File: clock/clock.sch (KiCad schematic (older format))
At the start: 63 parts, among them J1 Barrel_Jack, SW1 SW_Clock, SW2 CLK_SEL, SW3 SW_Step, SW4 SW_MANUAL_CLK, U1 LM7805, U10 LM555, U2 74LS93, U3 LM556, U4 74LS151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

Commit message: Added switches and redesign
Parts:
- removed C9: 10pF, Capacitor_THT:C_Disc_D3.8mm_W2.6mm_P2.50mm, symbol Device:C
- removed D14, D4: LED_Small, digikey-footprints:LED_3mm_Radial, symbol Device:LED_Small
- removed unit 1 of U5
- removed unit 4 of U5
- removed unit 5 of U5
- removed unit 1 of U6
- removed unit 2 of U7
- removed unit 3 of U7
- removed unit 4 of U7
- removed unit 5 of U7
- added J2: Conn_01x04, Connector_JST:JST_EH_B4B-EH-A_1x04_P2.50mm_Vertical, symbol Connector_Generic:Conn_01x04
- added Q1, Q2, Q3, Q4: 2N3904, Package_TO_SOT_THT:TO-92_Inline, symbol Transistor_BJT:2N3904
- added R17, R18, R19, R20: 1K, Resistor_THT:R_Axial_DIN0207_L6.3mm_D2.5mm_P7.62mm_Horizontal, symbol Device:R
- added RN3: 10K, Resistor_THT:R_Array_SIP5, symbol Device:R_Network04
- added U5: 74LS08, Package_DIP:DIP-14_W7.62mm_Socket, symbol 74xx:74LS08
- added unit 4 of U8
- added unit 5 of U8
- D1, D10, D11, D12, D13, D15, D2, D3, D5, D6, D7, D8, D9: footprint digikey-footprints:LED_3mm_Radial -> LED_THT:LED_D4.0mm
- R16: footprint Resistor_THT:R_Axial_DIN0204_L3.6mm_D1.6mm_P7.62mm_Horizontal -> Resistor_THT:R_Axial_DIN0207_L6.3mm_D2.5mm_P7.62mm_Horizontal
- RN1: value R_Network04 -> 470
- RN2: footprint Resistor_THT:R_Array_SIP6 -> Resistor_THT:R_Array_SIP5; symbol Device:R_Network05 -> Device:R_Network04
- U6: renamed from U7; value 74LS02 -> 74LS32; symbol 74xx:74LS02 -> 74xx:74LS32
- renumbered U5 to U9
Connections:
- net labels removed: PUL3
- wire segments 246 -> 261
- no-connect marks 4 -> 6
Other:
- moved on the sheet: D10, D11, D12, D13, U8A, U8C, U9A, U9B, U9D

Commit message: Fixed plug sizes and foot prints
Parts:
- added D4: D, Diode_THT:D_DO-41_SOD81_P7.62mm_Horizontal, symbol Device:D
- added J3: Power +5V In, Connector_JST:JST_EH_B2B-EH-A_1x02_P2.50mm_Vertical, symbol Connector_Generic:Conn_01x02
- J1: footprint Connector_BarrelJack:BarrelJack_CUI_PJ-063AH_Horizontal -> Connector_BarrelJack:BarrelJack_CUI_PJ-102AH_Horizontal
- J2: footprint Connector_JST:JST_EH_B4B-EH-A_1x04_P2.50mm_Vertical -> Connector_JST:JST_EH_B5B-EH-A_1x05_P2.50mm_Vertical; symbol Connector_Generic:Conn_01x04 -> Connector_Generic:Conn_01x05
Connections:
- wire segments 261 -> 274
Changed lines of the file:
@@
 F 0 "J1" H 850 7500 50  0000 C CNN
 F 1 "Barrel_Jack" H 850 7100 50  0001 C CNN
-F 2 "Connector_BarrelJack:BarrelJack_CUI_PJ-063AH_Horizontal" H 900 7260 50  0001 C CNN
+F 2 "Connector_BarrelJack:BarrelJack_CUI_PJ-102AH_Horizontal" H 900 7260 50  0001 C CNN
 F 3 "~" H 900 7260 50  0001 C CNN
 	1    850  7300
@@
 	3750 3750 4500 3750
 $Comp
-L Connector_Generic:Conn_01x04 J2
+L Connector_Generic:Conn_01x05 J2
 U 1 1 5D4F2577
-P 10050 3000
-F 0 "J2" V 10150 2950 50  0000 L CNN
-F 1 "Conn_01x04" H 10130 2901 50  0001 L CNN
-F 2 "Connector_JST:JST_EH_B4B-EH-A_1x04_P2.50mm_Vertical" H 10050 3000 50  0001 C CNN
-F 3 "~" H 10050 3000 50  0001 C CNN
-	1    10050 3000
-	0    -1   1    0
+P 10400 3100
+F 0 "J2" V 10500 3050 50  0000 L CNN
+F 1 "Conn_01x04" H 10480 3001 50  0001 L CNN
+F 2 "Connector_JST:JST_EH_B5B-EH-A_1x05_P2.50mm_Vertical" H 10400 3100 50  0001 C CNN
+F 3 "~" H 10400 3100 50  0001 C CNN
+	1    10400 3100
+	1    0    0    1
 $EndComp
 $Comp
@@
 $EndComp
 Wire Wire Line
-	9950 2600 9950 2800
+	9950 2600 9950 3200
 Wire Wire Line
 	10050 2150 10050 2650
@@
 Connection ~ 10250 2750
 Wire Wire Line
-	10250 2750 10250 2800
+	10250 2750 10250 2850
 Wire Wire Line
 	9650 2750 9650 2700
@@
 Connection ~ 10150 2700
 Wire Wire Line
-	10150 2700 10150 2800
+	10150 2700 10150 3000
 Wire Wire Line
 	9550 2750 9550 2650
@@
 Connection ~ 10050 2650
 Wire Wire Line
-	10050 2650 10050 2800
+	10050 2650 10050 3100
 Wire Wire Line
 	9450 2750 9450 2600
@@
 Wire Wire Line
 	10250 950  10250 800
+$Comp
+L Connector_Generic:Conn_01x02 J3
+U 1 1 5D72A18A
+P 3150 7200
+F 0 "J3" H 3230 7192 50  0000 L CNN
+F 1 "Power +5V In" H 3230 7101 50  0000 L CNN
+F 2 "Connector_JST:JST_EH_B2B-EH-A_1x02_P2.50mm_Vertical" H 3150 7200 50  0001 C CNN
+F 3 "~" H 3150 7200 50  0001 C CNN
+	1    3150 7200
+	1    0    0    -1
+$EndComp
+Connection ~ 2200 7400
+$Comp
+L Device:D D4
+U 1 1 5D58E7DA
+P 2600 7250
+F 0 "D4" V 2554 7329 50  0000 L CNN
+F 1 "D" V 2645 7329 50  0000 L CNN
+F 2 "Diode_THT:D_DO-41_SOD81_P7.62mm_Horizontal" H 2600 7250 50  0001 C CNN
+F 3 "~" H 2600 7250 50  0001 C CNN
+	1    2600 7250
+	0    1    1    0
+$EndComp
+Wire Wire Line
+	2200 7400 2600 7400
+Wire Wire Line
+	2600 7400 2950 7400
+Wire Wire Line
+	2950 7400 2950 7300
+Connection ~ 2600 7400
+Wire Wire Line
+	2950 7200 2950 7100
+Wire Wire Line
+	2950 7100 2600 7100
+Wire Wire Line
+	2200 7100 2600 7100
+Connection ~ 2600 7100
+Wire Wire Line
+	10200 3300 9750 3300
+Wire Wire Line
+	9750 3300 9750 3150
+Connection ~ 9750 3150
+Wire Wire Line
+	9950 3200 10200 3200
+Wire Wire Line
+	10050 3100 10200 3100
+Wire Wire Line
+	10150 3000 10200 3000
+Wire Wire Line
+	10200 2900 10200 2850
+Wire Wire Line
+	10200 2850 10250 2850
 $EndSCHEMATC

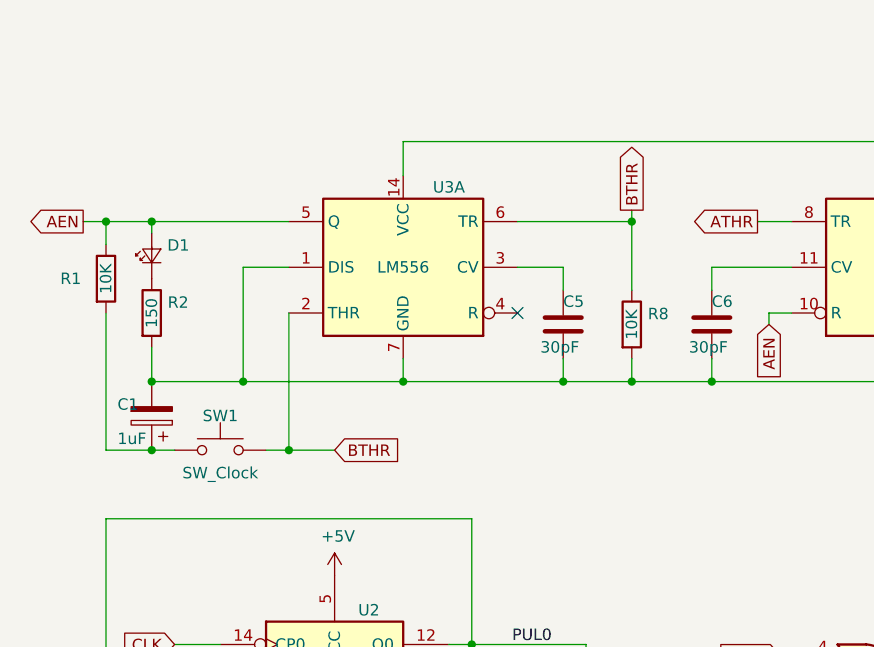
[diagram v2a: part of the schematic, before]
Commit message: Corrected LM556 toggle switch circuit
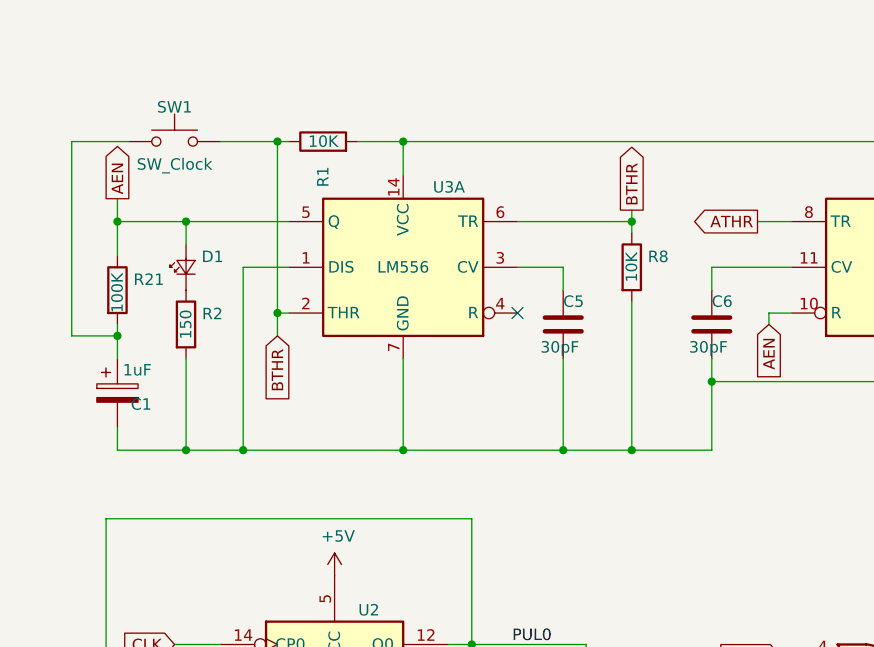
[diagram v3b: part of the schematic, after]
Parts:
- added R21: 100K, Resistor_THT:R_Axial_DIN0207_L6.3mm_D2.5mm_P7.62mm_Horizontal, symbol Device:R
- C7: footprint Capacitor_THT:C_Disc_D3.8mm_W2.6mm_P2.50mm -> Capacitor_THT:CP_Radial_D4.0mm_P2.00mm
- J1: footprint Connector_BarrelJack:BarrelJack_CUI_PJ-102AH_Horizontal -> Connector_BarrelJack:BarrelJack_Horizontal
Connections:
- wire segments 274 -> 282
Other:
- moved on the sheet: C1, D1, R1, R2, R8, SW1
